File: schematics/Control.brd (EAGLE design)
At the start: 114 x 78.2 mm, 82 parts, among them IC1 THAT1646, IC2 THAT1646, IC3 LM317MABT, IC5 NE5532N, J4 NEUTRIK_NMJ6HCD2, J5 NEUTRIK_NMJ6HCD2

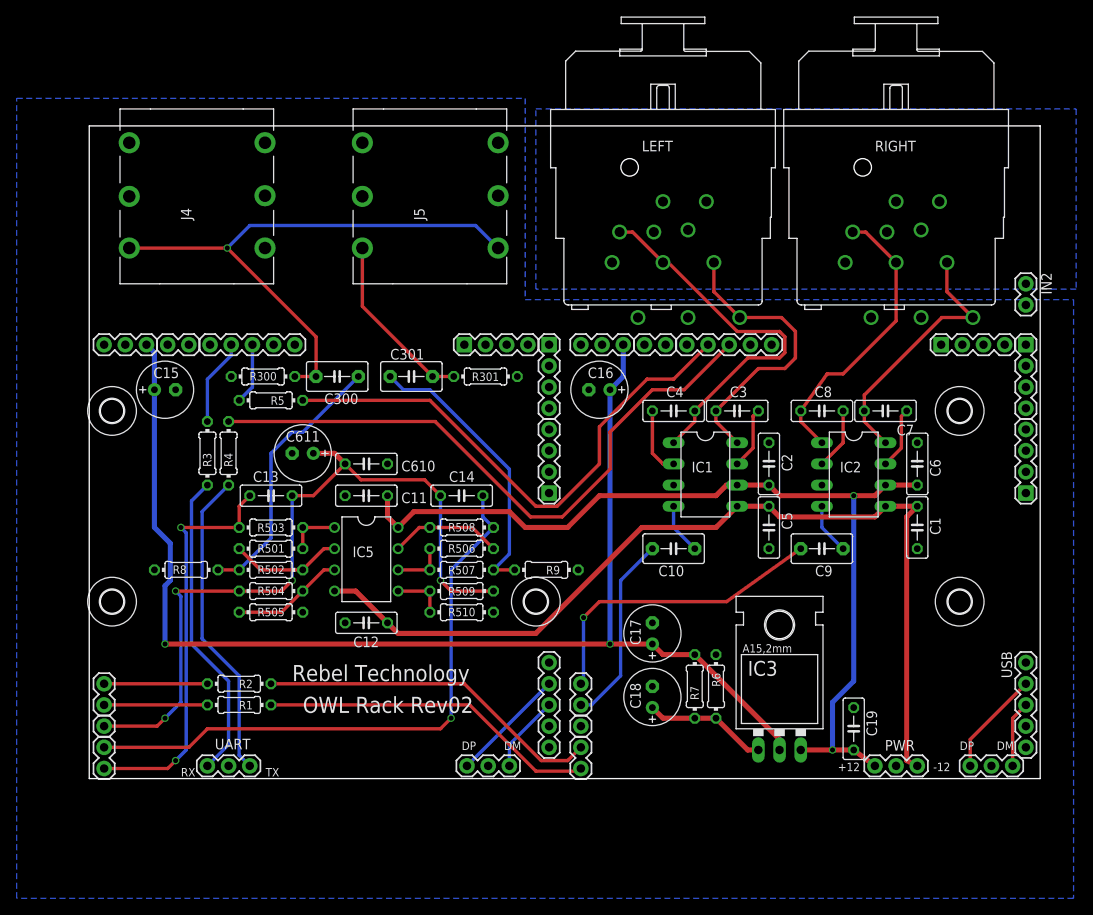
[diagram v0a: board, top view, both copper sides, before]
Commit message: added top polygon
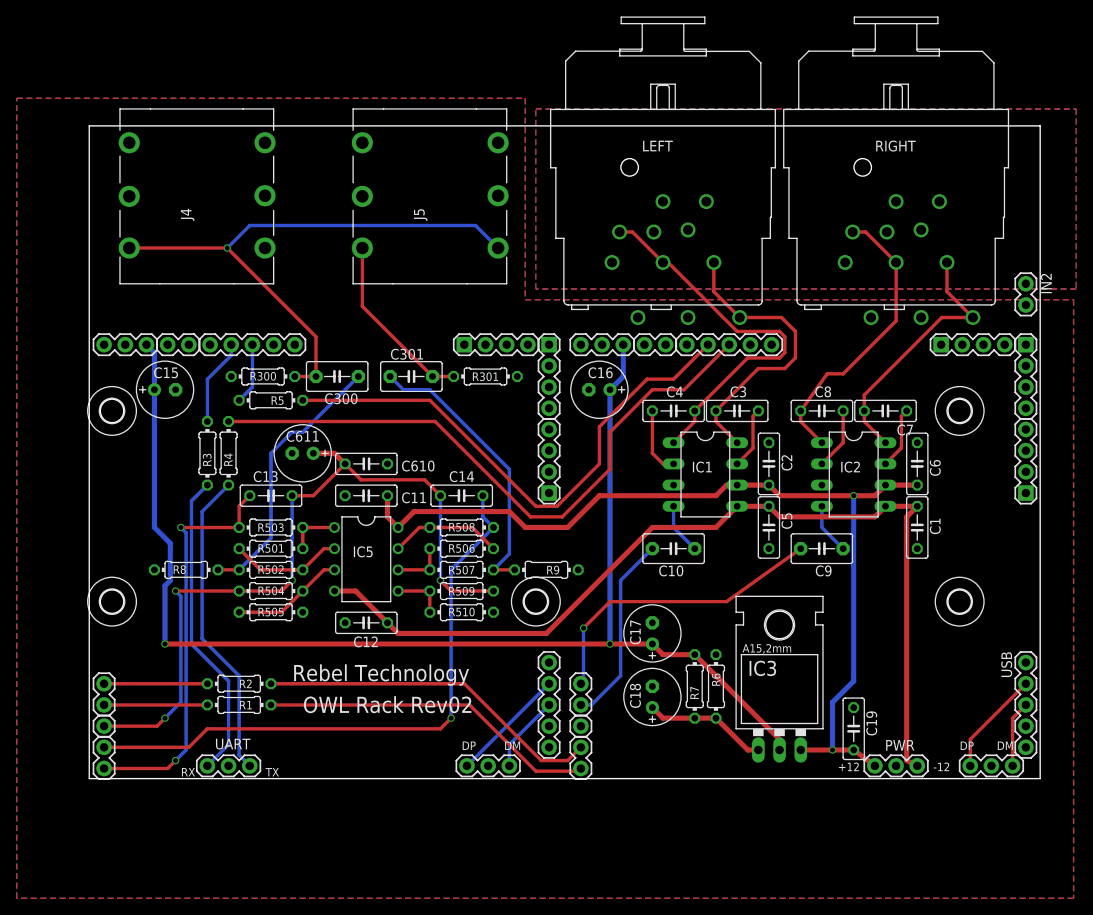
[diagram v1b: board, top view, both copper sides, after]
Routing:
- net R_OUT_A: track 36.9 -> 36.2 mm
- added copper zone on layer 1, net GND
- added copper zone on layer 1, net GNDA
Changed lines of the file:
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@@
 <contactref element="R8" pad="1"/>
 <contactref element="R9" pad="1"/>
+<polygon width="0.3048" layer="1">
+<vertex x="-7.62" y="8.255"/>
+<vertex x="-7.62" y="104.14"/>
+<vertex x="53.34" y="104.14"/>
+<vertex x="53.34" y="80.01"/>
+<vertex x="119.0625" y="80.01"/>
+<vertex x="119.0625" y="8.255"/>
+</polygon>
 </signal>
 <signal name="+5V">
@@
 <wire x1="99.06" y1="53.975" x2="100.33" y2="55.245" width="0.6096" layer="1"/>
 <wire x1="36.83" y1="41.275" x2="38.1" y2="40.005" width="0.6096" layer="1"/>
-<wire x1="38.1" y1="40.005" x2="54.61" y2="40.005" width="0.6096" layer="1"/>
-<wire x1="54.61" y1="40.005" x2="67.31" y2="52.705" width="0.6096" layer="1"/>
-<wire x1="67.31" y1="52.705" x2="76.2" y2="52.705" width="0.6096" layer="1"/>
+<wire x1="38.1" y1="40.005" x2="55.88" y2="40.005" width="0.6096" layer="1"/>
+<wire x1="55.88" y1="40.005" x2="68.58" y2="52.705" width="0.6096" layer="1"/>
+<wire x1="68.58" y1="52.705" x2="76.2" y2="52.705" width="0.6096" layer="1"/>
 <wire x1="76.2" y1="52.705" x2="78.74" y2="55.245" width="0.6096" layer="1"/>
 <wire x1="30.48" y1="45.085" x2="33.02" y2="45.085" width="0.6096" layer="1"/>
@@
 <vertex x="119.38" y="81.28"/>
 </polygon>
+<polygon width="0.4064" layer="1">
+<vertex x="54.61" y="81.28"/>
+<vertex x="54.61" y="102.87"/>
+<vertex x="119.38" y="102.87"/>
+<vertex x="119.38" y="81.28"/>
+</polygon>
 </signal>
 <signal name="N$18">
@@
 <contactref element="C9" pad="2"/>
 <wire x1="86.36" y1="50.165" x2="77.47" y2="43.815" width="0.4064" layer="1"/>
-<wire x1="77.47" y1="43.815" x2="62.23" y2="43.815" width="0.4064" layer="1"/>
-<wire x1="62.23" y1="43.815" x2="60.325" y2="41.91" width="0.4064" layer="1"/>
-<via x="60.325" y="41.91" extent="1-16" drill="0.6"/>
-<wire x1="60.325" y1="41.91" x2="60.325" y2="34.29" width="0.4064" layer="16"/>
+<wire x1="77.47" y1="43.815" x2="63.5" y2="43.815" width="0.4064" layer="1"/>
+<wire x1="63.5" y1="43.815" x2="60.325" y2="40.64" width="0.4064" layer="1"/>
+<via x="60.325" y="40.64" extent="1-16" drill="0.6"/>
+<wire x1="60.325" y1="40.64" x2="60.325" y2="34.29" width="0.4064" layer="16"/>
 <wire x1="60.325" y1="34.29" x2="60.0075" y2="33.9725" width="0.4064" layer="16"/>
 </signal>
